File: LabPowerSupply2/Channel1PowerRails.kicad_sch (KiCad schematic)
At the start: 8 parts

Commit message: Beautifing the Schematic
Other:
- moved on the sheet: C1_5V1, C2_3V1, C3_5V1
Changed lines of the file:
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@@
     (comment 4 "This supplys the 5 volts and 3.3 volts rail for the primary digital")
   )
+  (junction (at 171.45 106.68) (diameter 0) (color 0 0 0 0)
+  )
   (junction (at 102.87 106.68) (diameter 0) (color 0 0 0 0)
   )
@@
   (junction (at 207.01 88.9) (diameter 0) (color 0 0 0 0)
   )
+  (junction (at 158.75 88.9) (diameter 0) (color 0 0 0 0)
+  )
   (junction (at 196.85 106.68) (diameter 0) (color 0 0 0 0)
   )
-  (junction (at 167.64 88.9) (diameter 0) (color 0 0 0 0)
-  )
   (junction (at 181.61 88.9) (diameter 0) (color 0 0 0 0)
   )
   (junction (at 181.61 106.68) (diameter 0) (color 0 0 0 0)
   )
-  (junction (at 167.64 106.68) (diameter 0) (color 0 0 0 0)
-  )
   (junction (at 143.51 88.9) (diameter 0) (color 0 0 0 0)
   )
+  (junction (at 171.45 88.9) (diameter 0) (color 0 0 0 0)
+  )
   (junction (at 102.87 88.9) (diameter 0) (color 0 0 0 0)
   )
-  (junction (at 154.94 88.9) (diameter 0) (color 0 0 0 0)
-  )
-  (wire (pts (xy 167.64 88.9) (xy 181.61 88.9))
-    (stroke (width 0) (type default) (color 0 0 0 0))
-  )
-  (wire (pts (xy 207.01 95.25) (xy 207.01 88.9))
+  (wire (pts (xy 207.01 93.98) (xy 207.01 88.9))
     (stroke (width 0) (type default) (color 0 0 0 0))
   )
@@
     (stroke (width 0) (type default) (color 0 0 0 0))
   )
+  (wire (pts (xy 171.45 106.68) (xy 181.61 106.68))
+    (stroke (width 0) (type default) (color 0 0 0 0))
+  )
   (wire (pts (xy 102.87 88.9) (xy 114.3 88.9))
     (stroke (width 0) (type default) (color 0 0 0 0))
@@
     (stroke (width 0) (type default) (color 0 0 0 0))
   )
-  (wire (pts (xy 154.94 99.06) (xy 137.16 99.06))
+  (wire (pts (xy 158.75 104.14) (xy 137.16 104.14))
     (stroke (width 0) (type default) (color 0 0 0 0))
   )
@@
     (stroke (width 0) (type default) (color 0 0 0 0))
   )
-  (wire (pts (xy 167.64 101.6) (xy 167.64 106.68))
+  (wire (pts (xy 171.45 101.6) (xy 171.45 106.68))
     (stroke (width 0) (type default) (color 0 0 0 0))
   )
@@
     (stroke (width 0) (type default) (color 0 0 0 0))
   )
-  (wire (pts (xy 137.16 99.06) (xy 137.16 93.98))
-    (stroke (width 0) (type default) (color 0 0 0 0))
-  )
-  (wire (pts (xy 167.64 106.68) (xy 181.61 106.68))
-    (stroke (width 0) (type default) (color 0 0 0 0))
-  )
-  (wire (pts (xy 207.01 102.87) (xy 207.01 106.68))
+  (wire (pts (xy 137.16 104.14) (xy 137.16 93.98))
+    (stroke (width 0) (type default) (color 0 0 0 0))
+  )
+  (wire (pts (xy 207.01 101.6) (xy 207.01 106.68))
     (stroke (width 0) (type default) (color 0 0 0 0))
   )
@@
     (stroke (width 0) (type default) (color 0 0 0 0))
   )
-  (wire (pts (xy 102.87 104.14) (xy 102.87 106.68))
+  (wire (pts (xy 102.87 101.6) (xy 102.87 106.68))
     (stroke (width 0) (type default) (color 0 0 0 0))
   )
@@
     (stroke (width 0) (type default) (color 0 0 0 0))
   )
-  (wire (pts (xy 154.94 88.9) (xy 167.64 88.9))
+  (wire (pts (xy 153.67 88.9) (xy 158.75 88.9))
     (stroke (width 0) (type default) (color 0 0 0 0))
   )
@@
     (stroke (width 0) (type default) (color 0 0 0 0))
   )
-  (wire (pts (xy 167.64 88.9) (xy 167.64 93.98))
+  (wire (pts (xy 171.45 88.9) (xy 171.45 93.98))
+    (stroke (width 0) (type default) (color 0 0 0 0))
+  )
+  (wire (pts (xy 171.45 85.09) (xy 171.45 88.9))
+    (stroke (width 0) (type default) (color 0 0 0 0))
+  )
+  (wire (pts (xy 171.45 88.9) (xy 181.61 88.9))
+    (stroke (width 0) (type default) (color 0 0 0 0))
+  )
+  (wire (pts (xy 124.46 106.68) (xy 171.45 106.68))
     (stroke (width 0) (type default) (color 0 0 0 0))
   )
@@
     (stroke (width 0) (type default) (color 0 0 0 0))
   )
-  (wire (pts (xy 102.87 96.52) (xy 102.87 88.9))
-    (stroke (width 0) (type default) (color 0 0 0 0))
-  )
-  (wire (pts (xy 167.64 85.09) (xy 167.64 88.9))
+  (wire (pts (xy 102.87 93.98) (xy 102.87 88.9))
     (stroke (width 0) (type default) (color 0 0 0 0))
   )
@@
     (stroke (width 0) (type default) (color 0 0 0 0))
   )
-  (wire (pts (xy 154.94 88.9) (xy 154.94 99.06))
+  (wire (pts (xy 158.75 88.9) (xy 171.45 88.9))
+    (stroke (width 0) (type default) (color 0 0 0 0))
+  )
+  (wire (pts (xy 175.26 85.09) (xy 171.45 85.09))
+    (stroke (width 0) (type default) (color 0 0 0 0))
+  )
+  (wire (pts (xy 158.75 88.9) (xy 158.75 104.14))
     (stroke (width 0) (type default) (color 0 0 0 0))
   )
   (wire (pts (xy 102.87 106.68) (xy 124.46 106.68))
-    (stroke (width 0) (type default) (color 0 0 0 0))
-  )
-  (wire (pts (xy 124.46 106.68) (xy 167.64 106.68))
-    (stroke (width 0) (type default) (color 0 0 0 0))
-  )
-  (wire (pts (xy 153.67 88.9) (xy 154.94 88.9))
     (stroke (width 0) (type default) (color 0 0 0 0))
   )
@@
     (effects (font (size 1.27 1.27)) (justify right))
   )
-  (hierarchical_label "5 Volts" (shape output) (at 167.64 85.09 90)
+  (hierarchical_label "5 Volts" (shape output) (at 175.26 85.09 0)
     (effects (font (size 1.27 1.27)) (justify left))
   )
@@
     (pin "2")
   )
-  (symbol (lib_id "Device:C") (at 207.01 99.06 0) (unit 1)
-    (in_bom yes) (on_board yes) (fields_autoplaced)
-    (property "Reference" "C2_3V1" (id 0) (at 210.82 97.7899 0)
+  (symbol (lib_id "Device:C") (at 207.01 97.79 0) (unit 1)
+    (in_bom yes) (on_board yes) (fields_autoplaced)
+    (property "Reference" "C2_3V1" (id 0) (at 210.82 96.5199 0)
       (effects (font (size 1.27 1.27)) (justify left))
     )
-    (property "Value" "2.2u" (id 1) (at 210.82 100.3299 0)
+    (property "Value" "2.2u" (id 1) (at 210.82 99.0599 0)
       (effects (font (size 1.27 1.27)) (justify left))
     )
-    (property "Footprint" "Capacitor_SMD:C_0805_2012Metric" (id 2) (at 207.9752 102.87 0)
-      (effects (font (size 1.27 1.27)) hide)
-    )
-    (property "Datasheet" "~" (id 3) (at 207.01 99.06 0)
+    (property "Footprint" "Capacitor_SMD:C_0805_2012Metric" (id 2) (at 207.9752 101.6 0)
+      (effects (font (size 1.27 1.27)) hide)
+    )
+    (property "Datasheet" "~" (id 3) (at 207.01 97.79 0)
       (effects (font (size 1.27 1.27)) hide)
     )
@@
     (pin "3")
   )
-  (symbol (lib_id "Device:C") (at 102.87 100.33 0) (mirror x) (unit 1)
-    (in_bom yes) (on_board yes) (fields_autoplaced)
-    (property "Reference" "C1_5V1" (id 0) (at 99.06 99.0599 0)
-      (effects (font (size 1.27 1.27)) (justify right))
-    )
-    (property "Value" "10u" (id 1) (at 99.06 101.5999 0)
-      (effects (font (size 1.27 1.27)) (justify right))
-    )
-    (property "Footprint" "Capacitor_SMD:C_1206_3216Metric" (id 2) (at 103.8352 96.52 0)
-      (effects (font (size 1.27 1.27)) hide)
-    )
-    (property "Datasheet" "~" (id 3) (at 102.87 100.33 0)
-      (effects (font (size 1.27 1.27)) hide)
-    )
-    (pin "1")
-    (pin "2")
-  )
-  (symbol (lib_id "Device:C") (at 167.64 97.79 0) (mirror x) (unit 1)
-    (in_bom yes) (on_board yes) (fields_autoplaced)
-    (property "Reference" "C3_5V1" (id 0) (at 163.83 96.5199 0)
-      (effects (font (size 1.27 1.27)) (justify right))
-    )
-    (property "Value" "22u" (id 1) (at 163.83 99.0599 0)
-      (effects (font (size 1.27 1.27)) (justify right))
-    )
-    (property "Footprint" "Capacitor_SMD:C_1210_3225Metric" (id 2) (at 168.6052 93.98 0)
-      (effects (font (size 1.27 1.27)) hide)
-    )
-    (property "Datasheet" "~" (id 3) (at 167.64 97.79 0)
-      (effects (font (size 1.27 1.27)) hide)
-    )
+  (symbol (lib_id "Device:C") (at 102.87 97.79 0) (mirror x) (unit 1)
+    (in_bom yes) (on_board yes) (fields_autoplaced)
+    (property "Reference" "C1_5V1" (id 0) (at 99.06 96.5199 0)
+      (effects (font (size 1.27 1.27)) (justify right))
+    )
+    (property "Value" "10u" (id 1) (at 99.06 99.0599 0)
+      (effects (font (size 1.27 1.27)) (justify right))
+    )
+    (property "Footprint" "Capacitor_SMD:C_1206_3216Metric" (id 2) (at 103.8352 93.98 0)
+      (effects (font (size 1.27 1.27)) hide)
+    )
+    (property "Datasheet" "~" (id 3) (at 102.87 97.79 0)
+      (effects (font (size 1.27 1.27)) hide)
+    )
+    (pin "1")
+    (pin "2")
+  )
+  (symbol (lib_id "Device:C") (at 171.45 97.79 0) (mirror x) (unit 1)
+    (in_bom yes) (on_board yes) (fields_autoplaced)
+    (property "Reference" "C3_5V1" (id 0) (at 167.64 96.5199 0)
+      (effects (font (size 1.27 1.27)) (justify right))
+    )
+    (property "Value" "22u" (id 1) (at 167.64 99.0599 0)
+      (effects (font (size 1.27 1.27)) (justify right))
+    )
+    (property "Footprint" "Capacitor_SMD:C_1210_3225Metric" (id 2) (at 172.4152 93.98 0)
+      (effects (font (size 1.27 1.27)) hide)
+    )
+    (property "Datasheet" "~" (id 3) (at 171.45 97.79 0)
+      (effects (font (size 1.27 1.27)) hide)
+    )

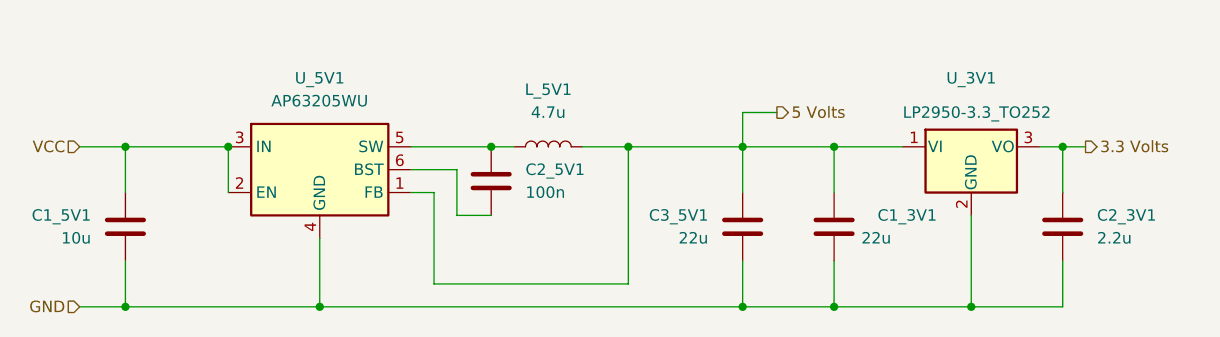
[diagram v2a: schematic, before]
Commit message: Fixed the Beautified Schematics
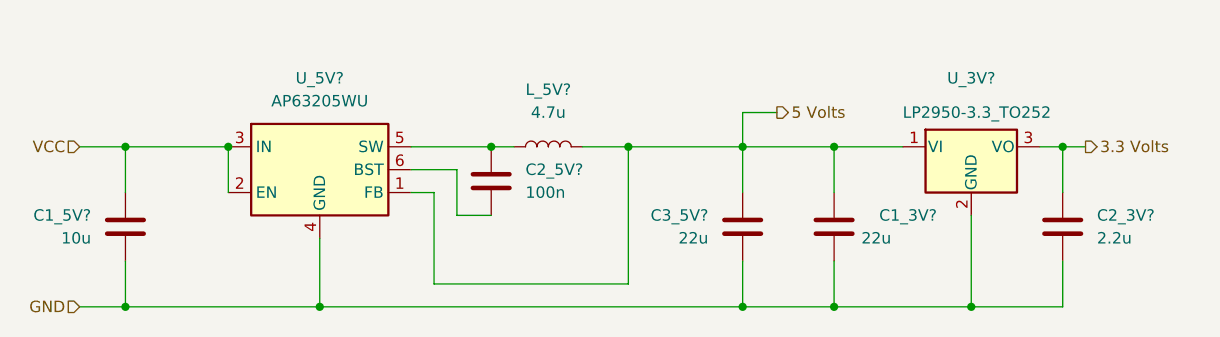
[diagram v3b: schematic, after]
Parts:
- renumbered C1_3V1 to C1_3V?, C1_5V1 to C1_5V?, C2_3V1 to C2_3V?, C2_5V1 to C2_5V?, C3_5V1 to C3_5V?, L_5V1 to L_5V?, U_3V1 to U_3V?, U_5V1 to U_5V?
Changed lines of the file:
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@@
   (symbol (lib_id "Device:C") (at 181.61 97.79 0) (mirror x) (unit 1)
     (in_bom yes) (on_board yes)
-    (property "Reference" "C1_3V1" (id 0) (at 193.04 96.52 0)
+    (property "Reference" "C1_3V?" (id 0) (at 193.04 96.52 0)
       (effects (font (size 1.27 1.27)) (justify right))
     )
@@
   (symbol (lib_id "Device:C") (at 207.01 97.79 0) (unit 1)
     (in_bom yes) (on_board yes) (fields_autoplaced)
-    (property "Reference" "C2_3V1" (id 0) (at 210.82 96.5199 0)
+    (property "Reference" "C2_3V?" (id 0) (at 210.82 96.5199 0)
       (effects (font (size 1.27 1.27)) (justify left))
     )
@@
   (symbol (lib_id "Device:L") (at 149.86 88.9 90) (unit 1)
     (in_bom yes) (on_board yes) (fields_autoplaced)
-    (property "Reference" "L_5V1" (id 0) (at 149.86 82.55 90))
+    (property "Reference" "L_5V?" (id 0) (at 149.86 82.55 90))
     (property "Value" "4.7u" (id 1) (at 149.86 85.09 90))
     (property "Footprint" "Inductor_SMD:L_Sumida_CDMC6D28_7.25x6.5mm" (id 2) (at 149.86 88.9 0)
@@
   (symbol (lib_id "Regulator_Linear:LP2950-3.3_TO252") (at 196.85 88.9 0) (unit 1)
     (in_bom yes) (on_board yes)
-    (property "Reference" "U_3V1" (id 0) (at 196.85 81.28 0))
+    (property "Reference" "U_3V?" (id 0) (at 196.85 81.28 0))
     (property "Value" "LP2950-3.3_TO252" (id 1) (at 189.23 85.09 0)
       (effects (font (size 1.27 1.27)) (justify left))
@@
   (symbol (lib_id "Device:C") (at 102.87 97.79 0) (mirror x) (unit 1)
     (in_bom yes) (on_board yes) (fields_autoplaced)
-    (property "Reference" "C1_5V1" (id 0) (at 99.06 96.5199 0)
+    (property "Reference" "C1_5V?" (id 0) (at 99.06 96.5199 0)
       (effects (font (size 1.27 1.27)) (justify right))
     )
@@
   (symbol (lib_id "Device:C") (at 171.45 97.79 0) (mirror x) (unit 1)
     (in_bom yes) (on_board yes) (fields_autoplaced)
-    (property "Reference" "C3_5V1" (id 0) (at 167.64 96.5199 0)
+    (property "Reference" "C3_5V?" (id 0) (at 167.64 96.5199 0)
       (effects (font (size 1.27 1.27)) (justify right))
     )
@@
   (symbol (lib_id "Device:C") (at 143.51 92.71 0) (unit 1)
     (in_bom yes) (on_board yes) (fields_autoplaced)
-    (property "Reference" "C2_5V1" (id 0) (at 147.32 91.4399 0)
+    (property "Reference" "C2_5V?" (id 0) (at 147.32 91.4399 0)
       (effects (font (size 1.27 1.27)) (justify left))
     )
@@
   (symbol (lib_id "Regulator_Switching:AP63205WU") (at 124.46 91.44 0) (unit 1)
     (in_bom yes) (on_board yes) (fields_autoplaced)
-    (property "Reference" "U_5V1" (id 0) (at 124.46 81.28 0))
+    (property "Reference" "U_5V?" (id 0) (at 124.46 81.28 0))
     (property "Value" "AP63205WU" (id 1) (at 124.46 83.82 0))
     (property "Footprint" "Package_TO_SOT_SMD:TSOT-23-6" (id 2) (at 124.46 114.3 0)
